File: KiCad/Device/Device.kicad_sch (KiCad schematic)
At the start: 27 parts, among them IC1 ATTINY167-XUR, J1 Mikrofon, J2 Lysføler, J3 Optisk sensor, J4 Fugtføler, J5 VCC, J6 ESP8266(wifi), SW1 Reset, SW2 Button01, SW3 SW_DIP_x01, Y1 Crystal

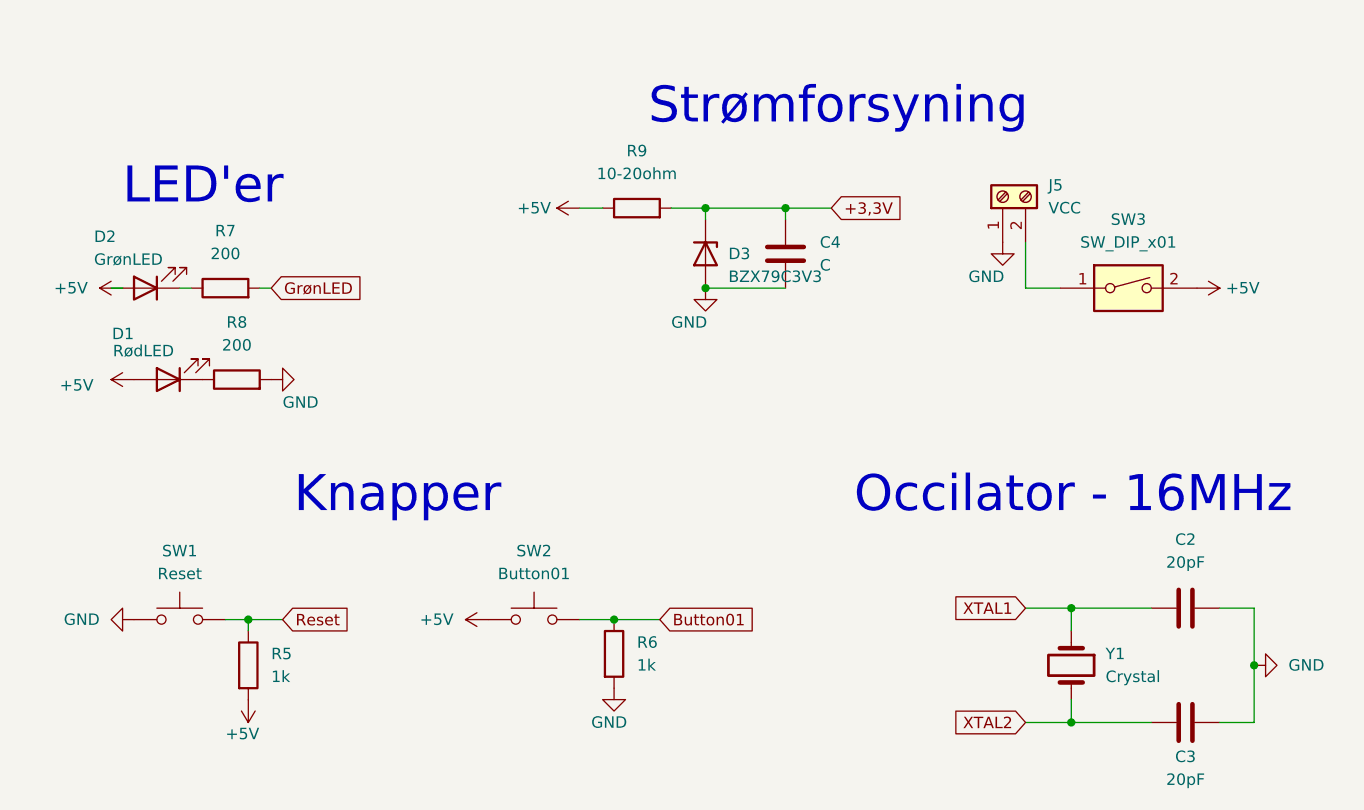
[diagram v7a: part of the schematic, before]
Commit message: Opdatering af switches
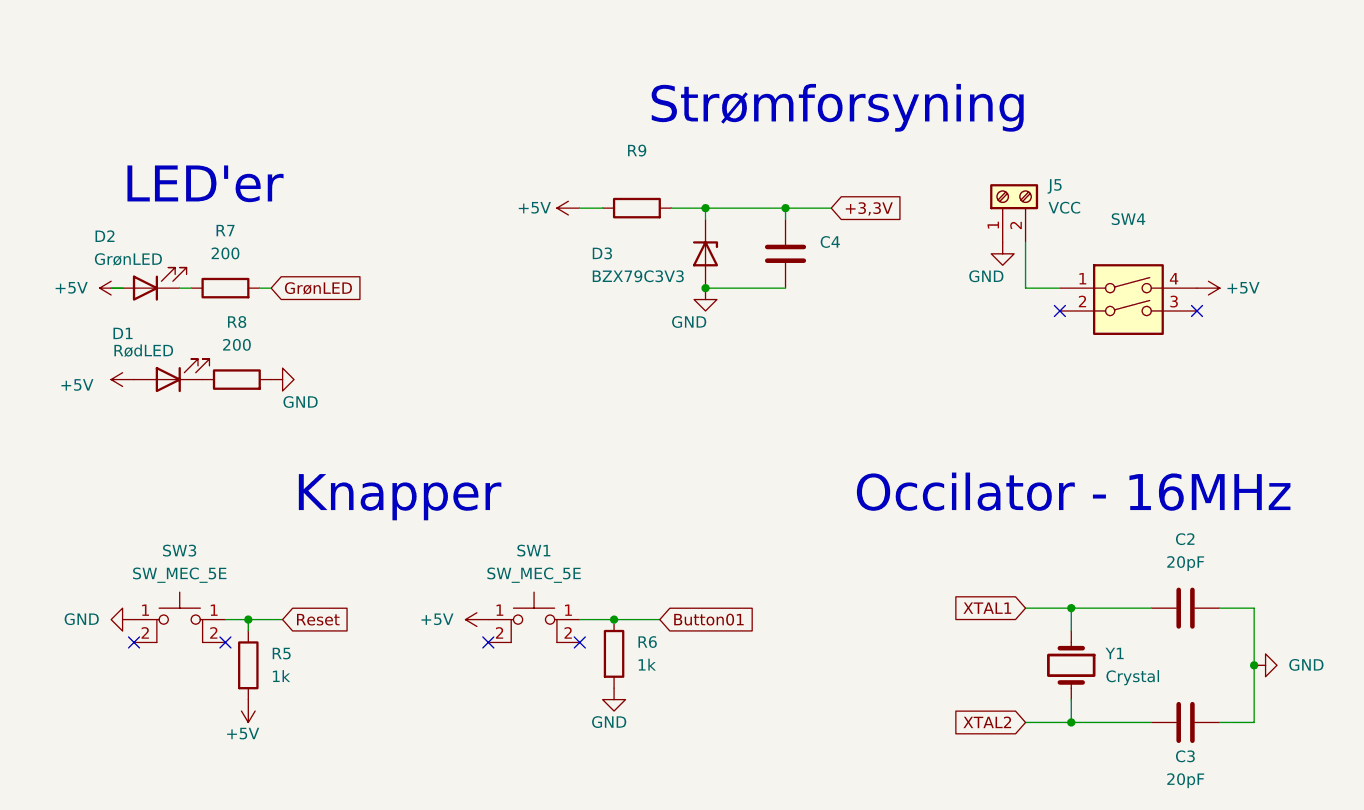
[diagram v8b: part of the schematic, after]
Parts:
- removed SW1: Reset, Button_Switch_THT:SW_PUSH_6mm_H4.3mm, symbol Switch:SW_MEC_5G
- removed SW2: Button01, Button_Switch_THT:SW_PUSH_6mm_H4.3mm, symbol Switch:SW_MEC_5G
- removed SW3: SW_DIP_x01, Button_Switch_THT:SW_DIP_SPSTx02_Slide_9.78x7.26mm_W7.62mm_P2.54mm, symbol Switch:SW_DIP_x01
- added SW1, SW3: SW_MEC_5E, Button_Switch_THT:SW_PUSH_6mm_H4.3mm, symbol Switch:SW_MEC_5E
- added SW4: (no value), symbol Switch:SW_DIP_x02
- C4: value C -> (none)
- R9: value 10-20ohm -> (none)
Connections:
- net +5V: now also SW1.1 (A), SW4.4
- net Button01: now also SW1.1 (A)
- net GND: now also SW3.1 (A)
- net Reset: now also SW3.1 (A)
- net at J5.2 (Pin_2): now also SW4.1
- no-connect marks 7 -> 13
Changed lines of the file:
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@@
   (junction (at 85.09 170.18) (diameter 0) (color 0 0 0 0)
   )
+  (no_connect (at 41.91 172.72))
+  (no_connect (at 31.75 172.72))
+  (no_connect (at 71.12 172.72))
+  (no_connect (at 81.28 172.72))
   (no_connect (at 201.93 125.73))
   (no_connect (at 236.22 52.07))
@@
   (no_connect (at 134.62 46.99))
   (no_connect (at 134.62 44.45))
+  (no_connect (at 134.62 135.89))
+  (no_connect (at 149.86 135.89))
   (no_connect (at 189.23 133.35))
   (wire (pts (xy 31.75 33.02) (xy 41.91 33.02))
@@
     )
     (pin "1")
+  )
+  (symbol (lib_name "SW_MEC_5E_1") (lib_id "Switch:SW_MEC_5E") (at 36.83 172.72 0) (unit 1)
+    (in_bom yes) (on_board yes) (fields_autoplaced)
+    (property "Reference" "SW3" (id 0) (at 36.83 162.56 0))
+    (property "Value" "SW_MEC_5E" (id 1) (at 36.83 165.1 0))
+    (property "Footprint" "Button_Switch_THT:SW_PUSH_6mm_H4.3mm" (id 2) (at 36.83 165.1 0)
+      (effects (font (size 1.27 1.27)) hide)
+    )
+    (property "Datasheet" "http://www.apem.com/int/index.php?controller=attachment&id_attachment=1371" (id 3) (at 36.83 165.1 0)
+      (effects (font (size 1.27 1.27)) hide)
+    )
+    (pin "1")
+    (pin "1")
+    (pin "2")
+    (pin "2")
   )
   (symbol (lib_name "ATTINY167-XUR_1") (lib_id "vitorkicad:ATTINY167-XUR") (at 134.62 44.45 0) (unit 1)
@@
     (pin "1")
   )
-  (symbol (lib_id "Switch:SW_DIP_x01") (at 142.24 133.35 0) (unit 1)
-    (in_bom yes) (on_board yes) (fields_autoplaced)
-    (property "Reference" "SW3" (id 0) (at 142.24 125.73 0))
-    (property "Value" "SW_DIP_x01" (id 1) (at 142.24 128.27 0))
-    (property "Footprint" "Button_Switch_THT:SW_DIP_SPSTx02_Slide_9.78x7.26mm_W7.62mm_P2.54mm" (id 2) (at 142.24 133.35 0)
-      (effects (font (size 1.27 1.27)) hide)
-    )
-    (property "Datasheet" "~" (id 3) (at 142.24 133.35 0)
-      (effects (font (size 1.27 1.27)) hide)
-    )
-    (pin "1")
-    (pin "2")
-  )
   (symbol (lib_id "Device:LED") (at 33.02 133.35 180) (unit 1)
     (in_bom yes) (on_board yes)
@@
     (pin "2")
   )
+  (symbol (lib_name "SW_MEC_5E_1") (lib_id "Switch:SW_MEC_5E") (at 76.2 172.72 0) (unit 1)
+    (in_bom yes) (on_board yes) (fields_autoplaced)
+    (property "Reference" "SW1" (id 0) (at 76.2 162.56 0))
+    (property "Value" "SW_MEC_5E" (id 1) (at 76.2 165.1 0))
+    (property "Footprint" "Button_Switch_THT:SW_PUSH_6mm_H4.3mm" (id 2) (at 76.2 165.1 0)
+      (effects (font (size 1.27 1.27)) hide)
+    )
+    (property "Datasheet" "http://www.apem.com/int/index.php?controller=attachment&id_attachment=1371" (id 3) (at 76.2 165.1 0)
+      (effects (font (size 1.27 1.27)) hide)
+    )
+    (pin "1")
+    (pin "1")
+    (pin "2")
+    (pin "2")
+  )
   (symbol (lib_id "Device:LED") (at 35.56 143.51 180) (unit 1)
     (in_bom yes) (on_board yes)
@@
       (effects (font (size 1.27 1.27)) (justify left))
     )
-    (property "Value" "C" (id 1) (at 107.95 130.8099 0)
+    (property "Value" "" (id 1) (at 107.95 130.8099 0)
       (effects (font (size 1.27 1.27)) (justify left))
     )
@@
     (pin "1")
   )
-  (symbol (lib_id "Switch:SW_MEC_5G") (at 76.2 170.18 0) (unit 1)
-    (in_bom yes) (on_board yes) (fields_autoplaced)
-    (property "Reference" "SW2" (id 0) (at 76.2 162.56 0))
-    (property "Value" "Button01" (id 1) (at 76.2 165.1 0))
-    (property "Footprint" "Button_Switch_THT:SW_PUSH_6mm_H4.3mm" (id 2) (at 76.2 165.1 0)
-      (effects (font (size 1.27 1.27)) hide)
-    )
-    (property "Datasheet" "http://www.apem.com/int/index.php?controller=attachment&id_attachment=488" (id 3) (at 76.2 165.1 0)
-      (effects (font (size 1.27 1.27)) hide)
-    )
-    (pin "1")
-    (pin "3")
-    (pin "2")
-    (pin "4")
-  )
   (symbol (lib_id "Device:C") (at 52.07 33.02 90) (unit 1)
     (in_bom yes) (on_board yes) (fields_autoplaced)
@@
     (pin "1")
   )
-  (symbol (lib_id "Switch:SW_MEC_5G") (at 36.83 170.18 0) (unit 1)
-    (in_bom yes) (on_board yes) (fields_autoplaced)
-    (property "Reference" "SW1" (id 0) (at 36.83 162.56 0))
-    (property "Value" "Reset" (id 1) (at 36.83 165.1 0))
-    (property "Footprint" "Button_Switch_THT:SW_PUSH_6mm_H4.3mm" (id 2) (at 36.83 165.1 0)
-      (effects (font (size 1.27 1.27)) hide)
-    )
-    (property "Datasheet" "http://www.apem.com/int/index.php?controller=attachment&id_attachment=488" (id 3) (at 36.83 165.1 0)
-      (effects (font (size 1.27 1.27)) hide)
-    )
-    (pin "1")
+  (symbol (lib_id "Switch:SW_DIP_x02") (at 142.24 135.89 0) (unit 1)
+    (in_bom yes) (on_board yes) (fields_autoplaced)
+    (property "Reference" "SW4" (id 0) (at 142.24 125.73 0))
+    (property "Value" "" (id 1) (at 142.24 128.27 0))
+    (property "Footprint" "" (id 2) (at 142.24 135.89 0)
+      (effects (font (size 1.27 1.27)) hide)
+    )
+    (property "Datasheet" "~" (id 3) (at 142.24 135.89 0)
+      (effects (font (size 1.27 1.27)) hide)
+    )
+    (pin "1")
+    (pin "2")
     (pin "3")
-    (pin "2")
     (pin "4")
   )
@@
     (in_bom yes) (on_board yes) (fields_autoplaced)
     (property "Reference" "R9" (id 0) (at 87.63 118.11 90))
-    (property "Value" "10-20ohm" (id 1) (at 87.63 120.65 90))
+    (property "Value" "" (id 1) (at 87.63 120.65 90))
     (property "Footprint" "Resistor_THT:R_Axial_DIN0309_L9.0mm_D3.2mm_P12.70mm_Horizontal" (id 2) (at 87.63 126.238 90)
       (effects (font (size 1.27 1.27)) hide)
@@
   (symbol (lib_id "Device:D_Zener") (at 95.25 129.54 270) (unit 1)
     (in_bom yes) (on_board yes)
-    (property "Reference" "D3" (id 0) (at 97.79 129.54 90)
-      (effects (font (size 1.27 1.27)) (justify left))
-    )
-    (property "Value" "BZX79C3V3" (id 1) (at 97.79 132.08 90)
+    (property "Reference" "D3" (id 0) (at 82.55 129.54 90)
+      (effects (font (size 1.27 1.27)) (justify left))
+    )
+    (property "Value" "BZX79C3V3" (id 1) (at 82.55 132.08 90)
       (effects (font (size 1.27 1.27)) (justify left))
     )
@@
     )
     (path "/956368da-6cbd-4b7b-b882-df53cc9e9a05"
-      (reference "C4") (unit 1) (value "C") (footprint "")
+      (reference "C4") (unit 1) (value "200n") (footprint "Capacitor_THT:C_Disc_D5.0mm_W2.5mm_P5.00mm")
     )
     (path "/7611e2c8-7c51-45ab-a61a-212ad250d6ba"
@@
     )
     (path "/e4e1e9dd-8530-4789-8ec3-4a96ec251638"
-      (reference "R9") (unit 1) (value "10-20ohm") (footprint "Resistor_THT:R_Axial_DIN0309_L9.0mm_D3.2mm_P12.70mm_Horizontal")
-    )
-    (path "/cd4f78c6-1905-45bc-8353-13fa5b012b26"
-      (reference "SW1") (unit 1) (value "Reset") (footprint "Button_Switch_THT:SW_PUSH_6mm_H4.3mm")
-    )
-    (path "/bb081121-b10a-47df-8559-7a1d3f99d968"
-      (reference "SW2") (unit 1) (value "Button01") (footprint "Button_Switch_THT:SW_PUSH_6mm_H4.3mm")
-    )
-    (path "/1f9cef0e-84ac-4eda-84fc-9f00d1d3d7b1"
-      (reference "SW3") (unit 1) (value "SW_DIP_x01") (footprint "Button_Switch_THT:SW_DIP_SPSTx02_Slide_9.78x7.26mm_W7.62mm_P2.54mm")
+      (reference "R9") (unit 1) (value "15") (footprint "Resistor_THT:R_Axial_DIN0309_L9.0mm_D3.2mm_P12.70mm_Horizontal")
+    )
+    (path "/7506efa9-5df8-46cb-afff-b1d7451aa89d"
+      (reference "SW1") (unit 1) (value "SW_MEC_5E") (footprint "Button_Switch_THT:SW_PUSH_6mm_H4.3mm")
+    )
+    (path "/15fdb793-f6db-4bc1-8f96-c3f606653097"
+      (reference "SW3") (unit 1) (value "SW_MEC_5E") (footprint "Button_Switch_THT:SW_PUSH_6mm_H4.3mm")
+    )
+    (path "/d2a546db-3fde-4450-a944-ed0a017a1804"
+      (reference "SW4") (unit 1) (value "SW_DIP_x02") (footprint "Button_Switch_THT:SW_DIP_SPSTx02_Slide_9.78x7.26mm_W7.62mm_P2.54mm")
     )
     (path "/5df0654c-8d6d-486d-b5f4-0be0de8af6ef"
